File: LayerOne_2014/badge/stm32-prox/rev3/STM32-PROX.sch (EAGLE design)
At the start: 268 parts, among them IC1 IC_TPS6120XQFN10, IC10 74XX244, IC105 MCP1824T-250, IC106 MCP1824T-120, IC11 CD4066, IC13 PQ1X331M2ZP-3V3-LDO-SOT-23-5, IC14 AD8052, IC2 STM32F1_HIGH_DENSITY_LQFP64LQ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, IC3 PQ1X331M2ZP-3V3-LDO-SOT-23-5, IC4 HCU-INVERTER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

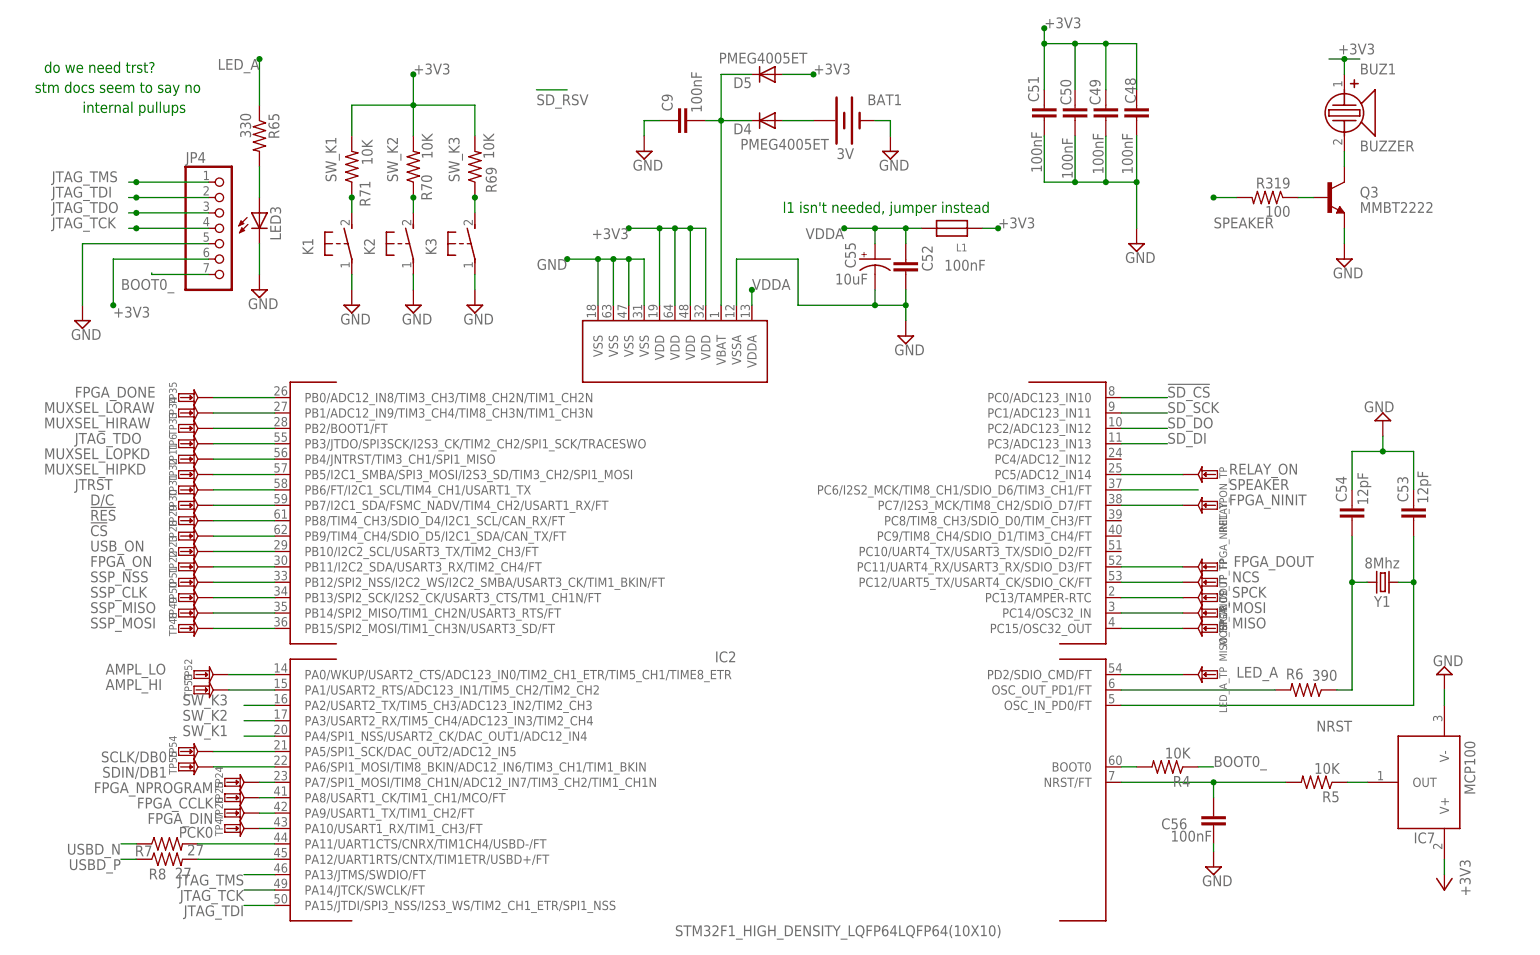
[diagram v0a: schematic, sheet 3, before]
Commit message: cpu changes, better layout moved caps.
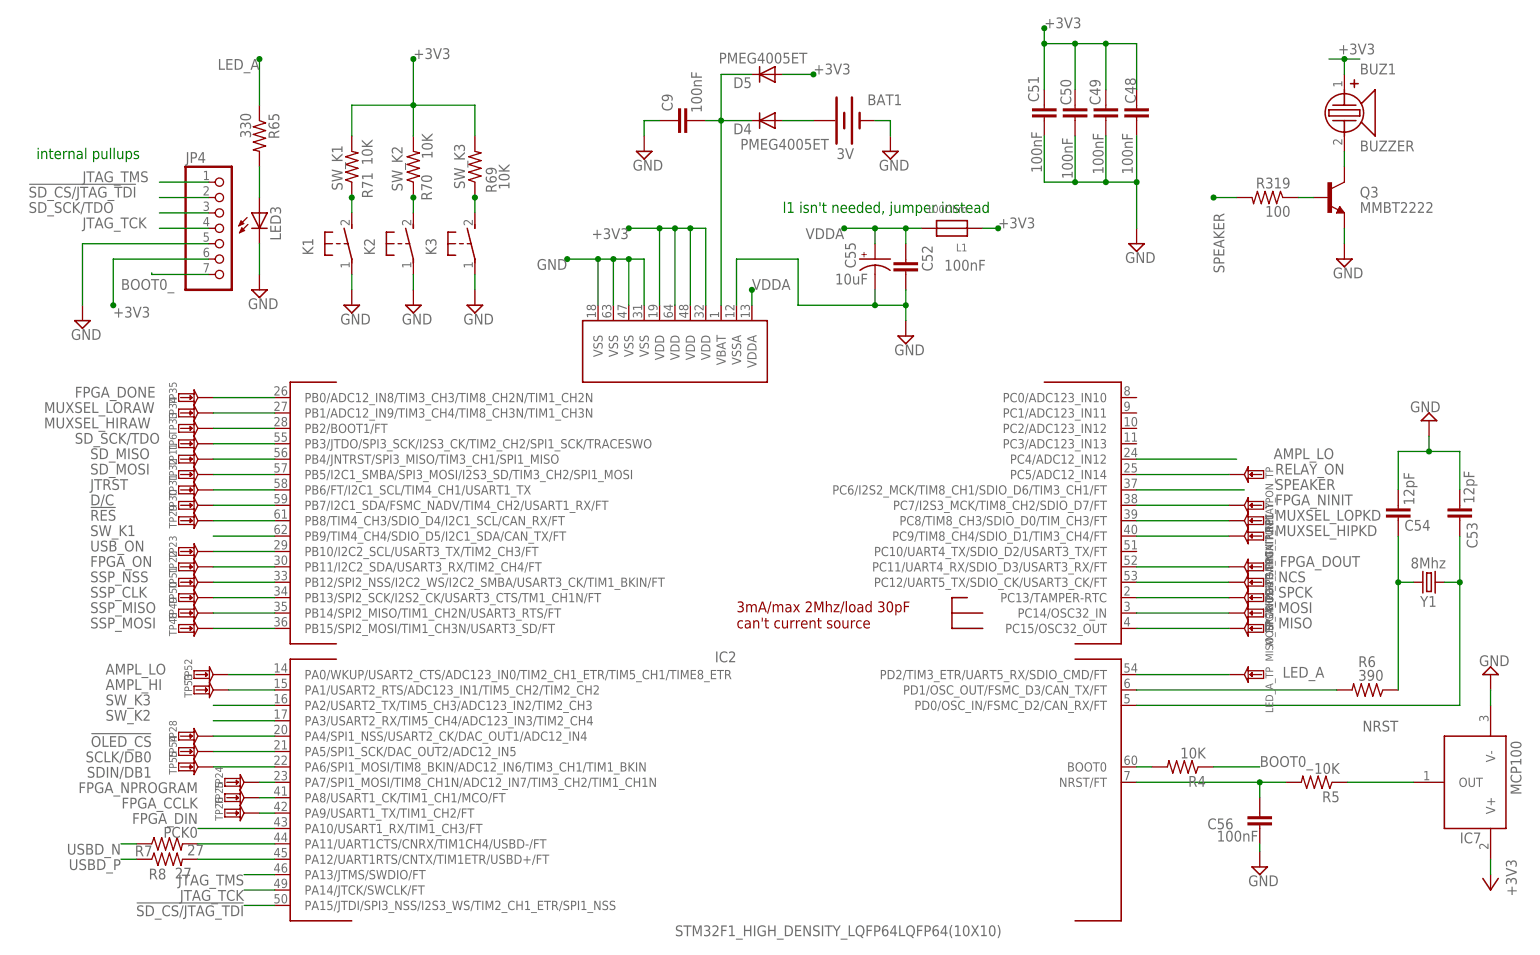
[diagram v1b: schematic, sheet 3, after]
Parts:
- removed TP47: TESTPAD, STM32-PROX:TESTPAD
- added FPGA_NINIT_TP1, FPGA_NINIT_TP2: TESTPAD, STM32-PROX:TESTPAD
- L1: value (none) -> 100Ohm
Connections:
- removed net !SD_CS: IC2.PC0/ADC123_IN10, R64.1, U4.CS
- removed net JTAG_TDI: IC2.PA15/JTDI/SPI3_NSS/I2S3_WS/TIM2_CH1_ETR/SPI1_NSS, JP4.2
- removed net JTAG_TDO: IC2.PB3/JTDO/SPI3SCK/I2S3_CK/TIM2_CH2/SPI1_SCK/TRACESWO, JP4.3, TP6.P$1
- removed net SD_DI: IC2.PC3/ADC123_IN13, R63.1, U4.DI
- removed net SD_DO: IC2.PC2/ADC123_IN12, R62.1, U4.DO
- removed net SD_SCK: IC2.PC1/ADC123_IN11, U4.SCK
- new net !OLED_CS: IC2.PA4/SPI1_NSS/USART2_CK/DAC_OUT1/ADC12_IN4, TP28.P$1
- new net !SD_CS/JTAG_TDI: IC2.PA15/JTDI/SPI3_NSS/I2S3_WS/TIM2_CH1_ETR/SPI1_NSS, JP4.2, R64.1, U4.CS
- new net SD_MISO: IC2.PB4/JNTRST/SPI3_MISO/TIM3_CH1/SPI1_MISO, R62.1, TP11.P$1, U4.DO
- new net SD_MOSI: IC2.PB5/I2C1_SMBA/SPI3_MOSI/I2S3_SD/TIM3_CH2/SPI1_MOSI, R63.1, TP32.P$1, U4.DI
- new net SD_SCK/TDO: IC2.PB3/JTDO/SPI3_SCK/I2S3_CK/TIM2_CH2/SPI1_SCK/TRACESWO, JP4.3, TP6.P$1, U4.SCK
- net !CS: no longer IC2.PB9/TIM4_CH4/SDIO_D5/I2C1_SDA/CAN_TX/FT, TP28.P$1
- net AMPL_LO: now also IC2.PC4/ADC12_IN12
- net FPGA_DOUT: now also IC2.PC11/UART4_RX/SDIO_D3/USART3_RX/FT; no longer IC2.PC11/UART4_RX/USART3_RX/SDIO_D3/FT
- net LED_A: now also IC2.PD2/TIM3_ETR/UART5_RX/SDIO_CMD/FT; no longer IC2.PD2/SDIO_CMD/FT
- net MUXSEL_HIPKD: now also FPGA_NINIT_TP2.P$1, IC2.PC9/TIM8_CH4/SDIO_D1/TIM3_CH4/FT; no longer IC2.PB5/I2C1_SMBA/SPI3_MOSI/I2S3_SD/TIM3_CH2/SPI1_MOSI, TP32.P$1
- net MUXSEL_LOPKD: now also FPGA_NINIT_TP1.P$1, IC2.PC8/TIM8_CH3/SDIO_D0/TIM_CH3/FT; no longer IC2.PB4/JNTRST/TIM3_CH1/SPI1_MISO, TP11.P$1
- net N$2: now also IC2.PD0/OSC_IN/FSMC_D2/CAN_RX/FT; no longer IC2.OSC_IN_PD0/FT
- net N$61: now also IC2.PD1/OSC_OUT/FSMC_D3/CAN_TX/FT; no longer IC2.OSC_OUT_PD1/FT
- net NCS: now also IC2.PC12/UART5_TX/SDIO_CK/USART3_CK/FT; no longer IC2.PC12/UART5_TX/USART4_CK/SDIO_CK/FT
- net PCK0: no longer TP47.P$1
- net SW_K1: now also IC2.PB9/TIM4_CH4/SDIO_D5/I2C1_SDA/CAN_TX/FT; no longer IC2.PA4/SPI1_NSS/USART2_CK/DAC_OUT1/ADC12_IN4
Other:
- note removed: "do we need trst?"
- note removed: "stm docs seem to say no"
- moved on the sheet: C53, C54, C56, FPGA_DOUT_TP, FPGA_NINIT_TP, IC7, LED_A_TP, MISO_TP, MOSI_TP, NCS_TP, R4, R6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

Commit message: selectable adc's
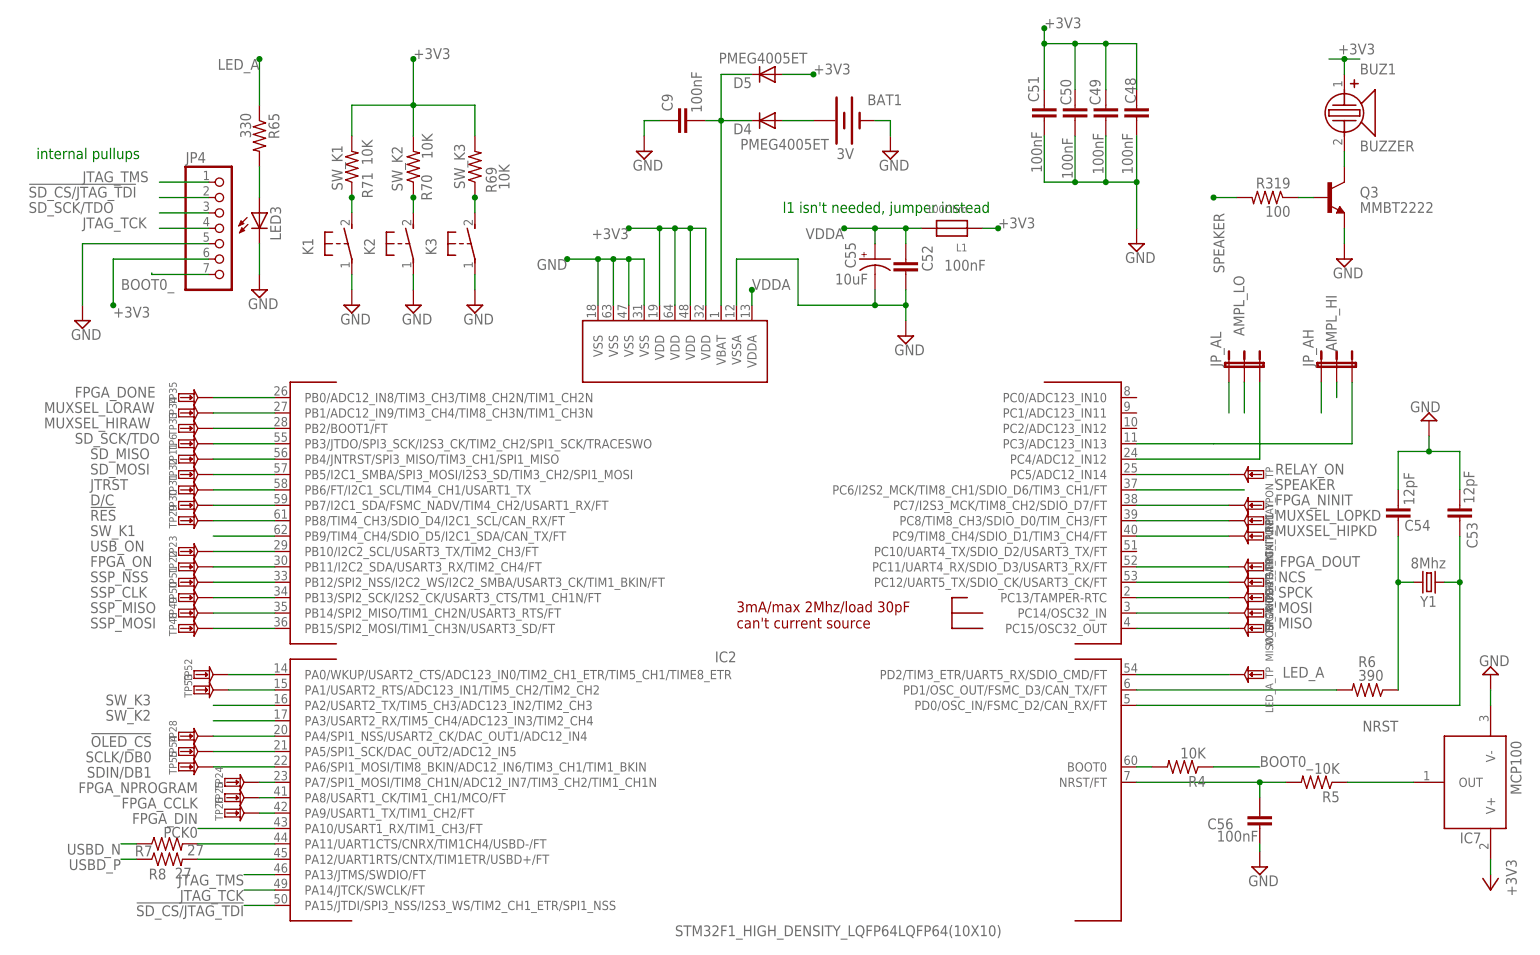
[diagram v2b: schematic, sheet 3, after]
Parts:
- added JP_AH, JP_AL: JUMPER-3SMD, STM32-PROX:JUMPER-3SMD
- DBG_TP: value TESTPAD -> TESTPADKEYSTONE-SMD; device STM32-PROX:TESTPAD -> STM32-PROX:TESTPADKEYSTONE-SMD
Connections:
- removed net !CS: U3./CS
- new net AMPL_HI1: IC2.PA1/USART2_RTS/ADC123_IN1/TIM5_CH2/TIM2_CH2, JP_AH.1, TP53.P$1
- new net AMPL_LO1: IC2.PA0/WKUP/USART2_CTS/ADC123_IN0/TIM2_CH1_ETR/TIM5_CH1/TIME8_ETR, JP_AL.1, TP52.P$1
- new net N$1: IC2.PC4/ADC12_IN12, JP_AL.3
- new net N$7: IC2.PC3/ADC123_IN13, JP_AH.3
- net !OLED_CS: now also U3./CS
- net AMPL_HI: now also JP_AH.2; no longer IC2.PA1/USART2_RTS/ADC123_IN1/TIM5_CH2/TIM2_CH2, TP53.P$1
- net AMPL_LO: now also JP_AL.2; no longer IC2.PA0/WKUP/USART2_CTS/ADC123_IN0/TIM2_CH1_ETR/TIM5_CH1/TIME8_ETR, IC2.PC4/ADC12_IN12, TP52.P$1

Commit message: schematic fixes.
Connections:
- net FPGA_NINIT: now also IC2.PC7/I2S3_MCK/TIM8_CH2/SDIO_D7/TIM3_CH2/FT; no longer IC2.PC7/I2S3_MCK/TIM8_CH2/SDIO_D7/FT
- net MUXSEL_LOPKD: now also IC2.PC8/TIM8_CH3/SDIO_D0/TIM3_CH3/FT; no longer IC2.PC8/TIM8_CH3/SDIO_D0/TIM_CH3/FT
- net N$1: now also IC2.PC4/ADC12_IN14; no longer IC2.PC4/ADC12_IN12
- net NRST: now also IC2.NRST; no longer IC2.NRST/FT
- net RELAY_ON: now also IC2.PC5/ADC12_IN15; no longer IC2.PC5/ADC12_IN14
- net SSP_CLK: now also IC2.PB13/SPI2_SCK/I2S2_CK/USART3_CTS/TIM1_CH1N/FT; no longer IC2.PB13/SPI2_SCK/I2S2_CK/USART3_CTS/TM1_CH1N/FT
- net SSP_MOSI: now also IC2.PB15/SPI2_MOSI/TIM1_CH3N/I2S2_SD/FT; no longer IC2.PB15/SPI2_MOSI/TIM1_CH3N/USART3_SD/FT
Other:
- moved on the sheet: BUZ1, JP_AH, JP_AL, Q3, R319, TP24, TP25, TP26, TP52, TP53

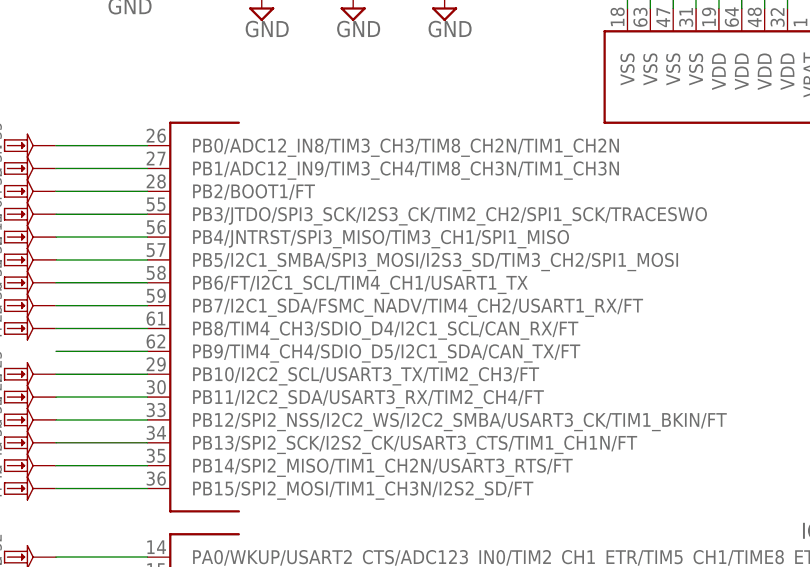
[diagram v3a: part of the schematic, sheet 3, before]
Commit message: 
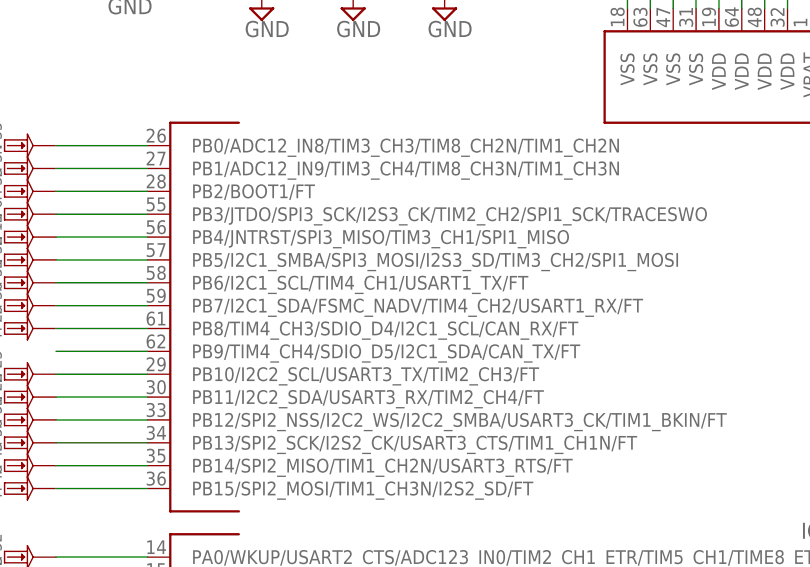
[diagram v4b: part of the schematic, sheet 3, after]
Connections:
- net JTRST: now also IC2.PB6/I2C1_SCL/TIM4_CH1/USART1_TX/FT; no longer IC2.PB6/FT/I2C1_SCL/TIM4_CH1/USART1_TX
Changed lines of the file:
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@@
 <wire x1="60.96" y1="55.88" x2="50.8" y2="55.88" width="0.1524" layer="91"/>
 <label x="30.48" y="55.88" size="1.778" layer="95"/>
-<pinref part="IC2" gate="G$1" pin="PB6/FT/I2C1_SCL/TIM4_CH1/USART1_TX"/>
+<pinref part="IC2" gate="G$1" pin="PB6/I2C1_SCL/TIM4_CH1/USART1_TX/FT"/>
 </segment>
 </net>
